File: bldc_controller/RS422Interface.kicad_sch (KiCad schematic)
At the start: 2 parts, among them U8 SN65HVD35DR

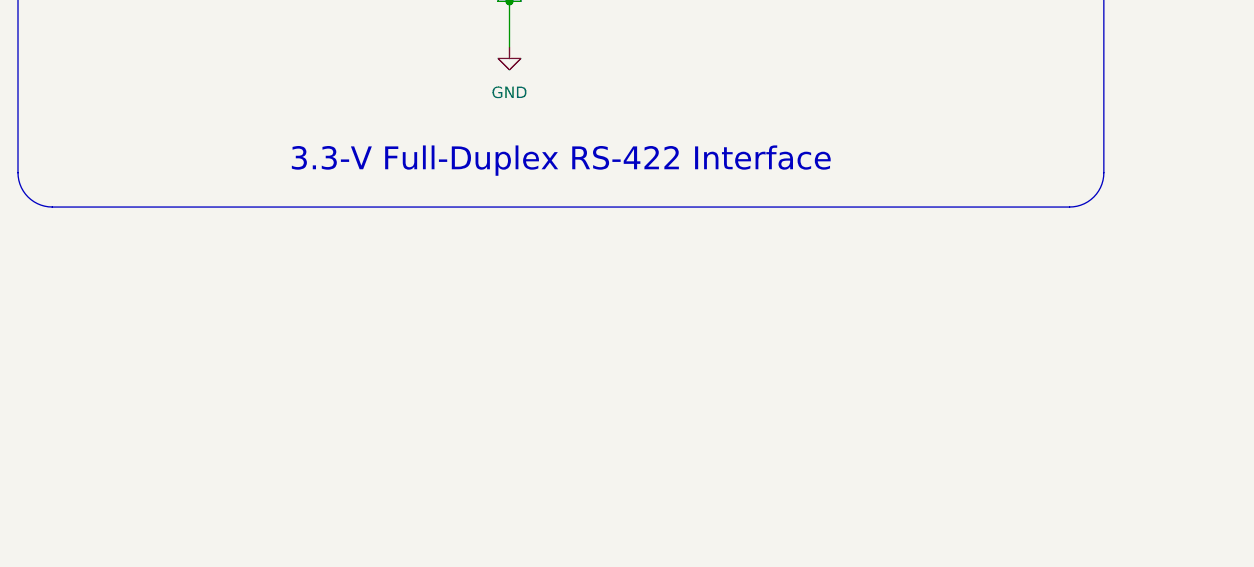
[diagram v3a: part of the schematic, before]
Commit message: Added TVS diodes to all interfaces
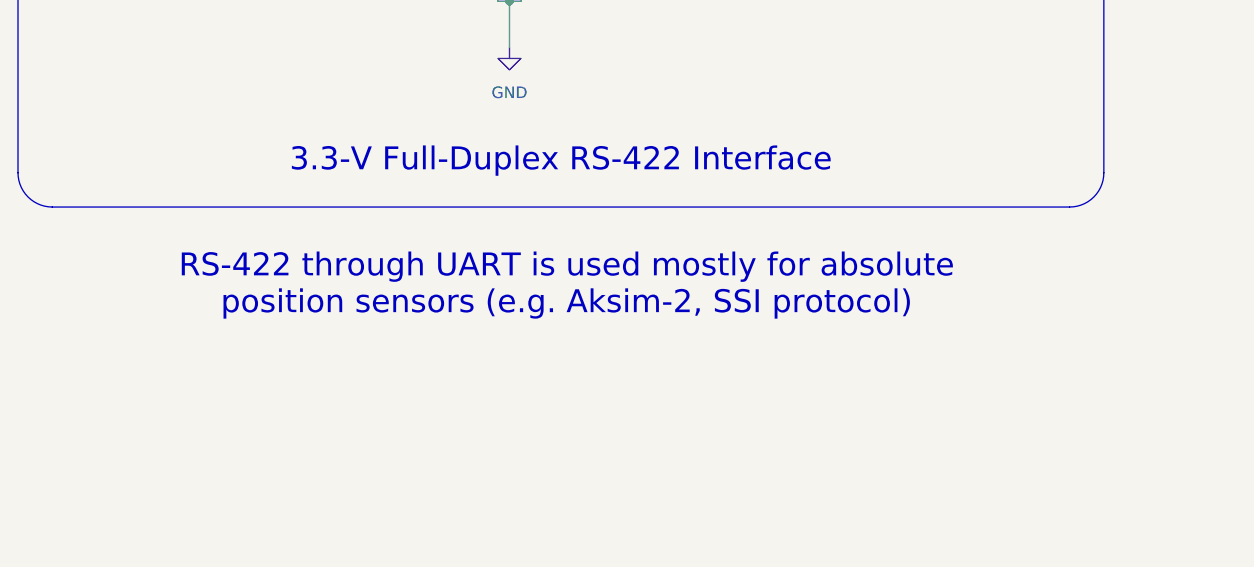
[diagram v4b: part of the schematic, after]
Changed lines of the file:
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@@
     (effects (font (size 1.27 1.27) (color 0 0 0 1)) (justify left))
+  )
+  (text_box "RS-422 through UART is used mostly for absolute position sensors (e.g. Aksim-2, SSI protocol)"
+    (at 92.71 133.35 0) (size 119.38 11.43)
+    (stroke (width -0.0001) (type default))
+    (fill (type none))
+    (effects (font (size 2.54 2.54) (color 0 0 0 1)) (justify bottom))
   )
   (text_box "3.3-V Full-Duplex RS-422 Interface"

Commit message: might have fixed net issue, added dxf and svgs
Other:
- moved on the sheet: C91, U8

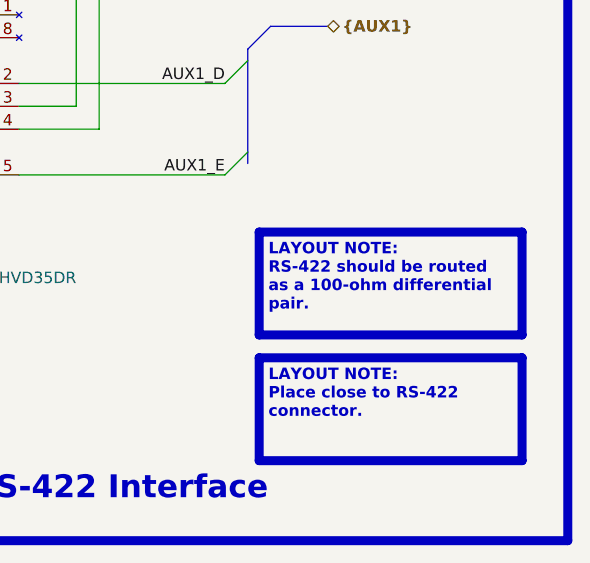
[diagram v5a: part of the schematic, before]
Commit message: added chassis connection to connector MP. Might need to change design rules to be compatible with low-cost PCBWay
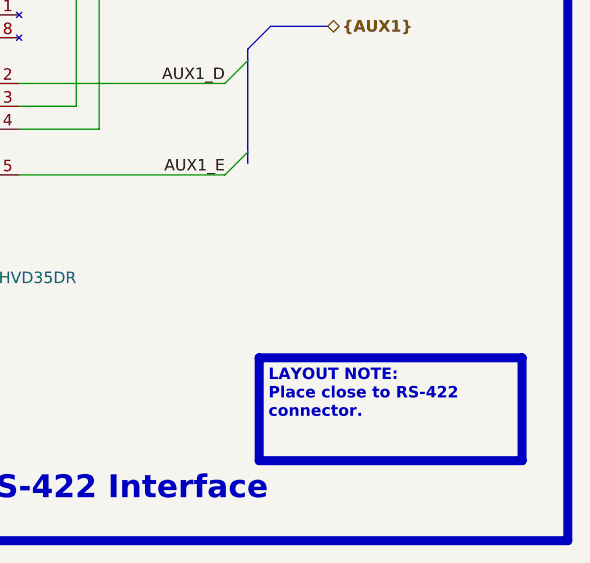
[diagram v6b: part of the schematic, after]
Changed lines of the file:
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@@
     (comment 3 "Author: Vincent Nguyen")
   )
-  (junction (at 146.05 104.14) (diameter 0) (color 0 0 0 0)
+  (junction (at 146.05 104.14) (diameter 0) (color 0 0 0 1)
   )
   (junction (at 147.32 54.61) (diameter 0) (color 0 0 0 0)
@@
   )
   (wire (pts (xy 146.05 104.14) (xy 147.32 104.14))
-    (stroke (width 0) (type default))
+    (stroke (width 0.381) (type default) (color 0 0 0 1))
   )
   (wire (pts (xy 147.32 54.61) (xy 147.32 62.23))
@@
   )
   (wire (pts (xy 144.78 104.14) (xy 144.78 102.87))
-    (stroke (width 0) (type default))
+    (stroke (width 0.381) (type default) (color 0 0 0 1))
   )
   (wire (pts (xy 144.78 62.23) (xy 144.78 64.77))
@@
   )
   (wire (pts (xy 128.27 64.77) (xy 128.27 62.23))
-    (stroke (width 0) (type default))
+    (stroke (width 0.381) (type default) (color 0 0 0 1))
   )
   (wire (pts (xy 128.27 54.61) (xy 147.32 54.61))
@@
   )
   (wire (pts (xy 147.32 102.87) (xy 147.32 104.14))
-    (stroke (width 0) (type default))
+    (stroke (width 0.381) (type default) (color 0 0 0 1))
   )
   (wire (pts (xy 162.56 62.23) (xy 179.07 62.23))
@@
   )
   (wire (pts (xy 146.05 104.14) (xy 144.78 104.14))
-    (stroke (width 0) (type default))
+    (stroke (width 0.381) (type default) (color 0 0 0 1))
   )
   (wire (pts (xy 146.05 109.22) (xy 146.05 104.14))
-    (stroke (width 0) (type default))
+    (stroke (width 0.381) (type default) (color 0 0 0 1))
   )
   (rectangle (start 82.55 41.91) (end 217.17 130.81)
@@
     (effects (font (face "Arial") (size 1.27 1.27) (color 0 0 0 1)) (justify left top))
   )
-  (text_box "LAYOUT NOTE:\nRS-422 should be routed as a 100-ohm differential pair."
-    (at 182.88 96.52 0) (size 29.21 11.43)
-    (stroke (width 1) (type solid) (color 0 0 255 1))
-    (fill (type none))
-    (effects (font (face "Arial") (size 1.27 1.27) (thickness 0.4) bold (color 0 0 255 1)) (justify left top))
-  )
   (text_box "DESIGN NOTE:\n100-ohm termination in Interconnects sheet."

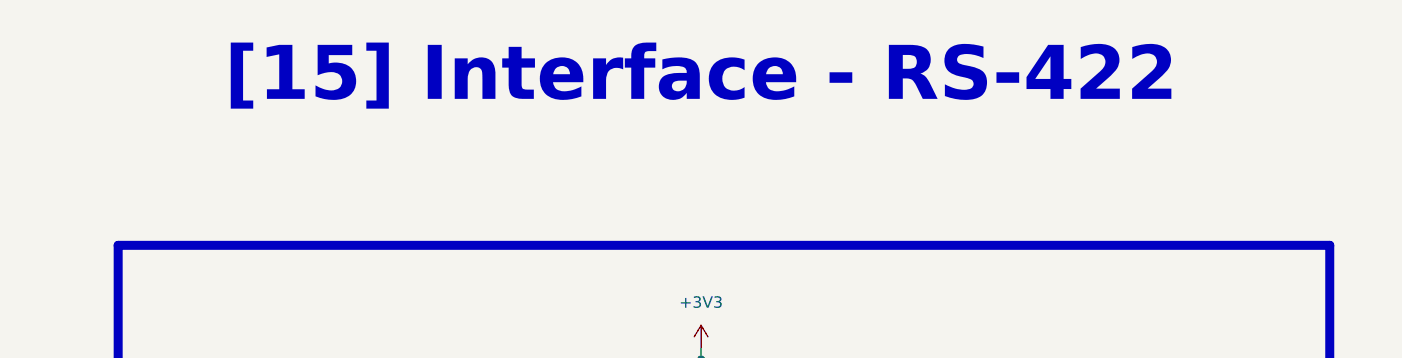
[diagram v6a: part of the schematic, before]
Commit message: Replaced 3v3 buck with WSON package alternative. Will back-annotate components
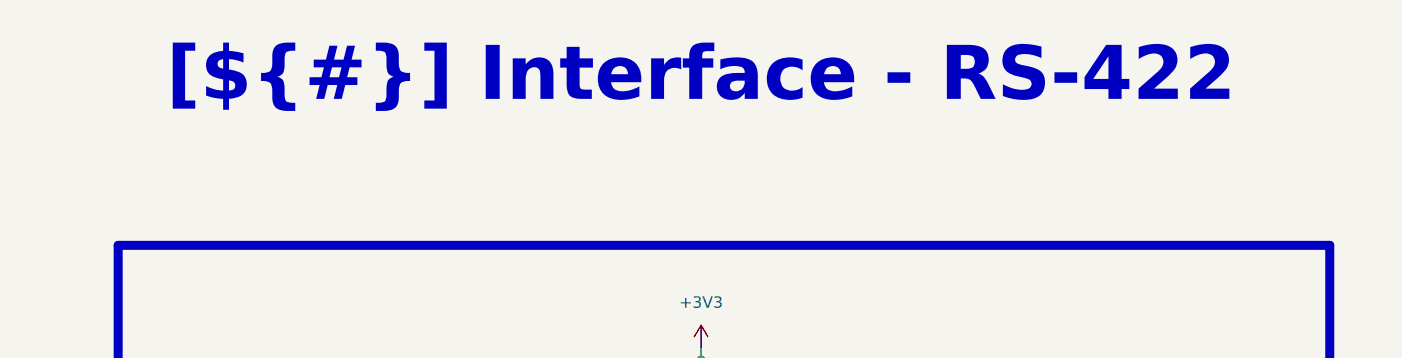
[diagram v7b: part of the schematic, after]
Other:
- company: EPFL Xplore -> ${COMPANY}
- title: RS-422 Interface -> Interface - RS-422
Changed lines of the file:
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@@
   (paper "A4")
   (title_block
-    (title "RS-422 Interface")
+    (title "Interface - RS-422")
     (date "2023-10-15")
-    (rev "1.0")
-    (company "EPFL Xplore")
-    (comment 3 "Author: Vincent Nguyen")
+    (rev "${REVISION}")
+    (company "${COMPANY}")
+    (comment 3 "Author: ${AUTHOR}")
   )
-  (junction (at 146.05 104.14) (diameter 0) (color 0 0 0 1)
+  (junction (at 146.05 104.14) (diameter 0) (color 0 0 0 0)
   )
   (junction (at 147.32 54.61) (diameter 0) (color 0 0 0 0)
@@
   )
   (wire (pts (xy 146.05 104.14) (xy 147.32 104.14))
-    (stroke (width 0.381) (type default) (color 0 0 0 1))
+    (stroke (width 0) (type default))
   )
   (wire (pts (xy 147.32 54.61) (xy 147.32 62.23))
@@
   )
   (wire (pts (xy 144.78 104.14) (xy 144.78 102.87))
-    (stroke (width 0.381) (type default) (color 0 0 0 1))
+    (stroke (width 0) (type default))
   )
   (wire (pts (xy 144.78 62.23) (xy 144.78 64.77))
@@
   )
   (wire (pts (xy 128.27 64.77) (xy 128.27 62.23))
-    (stroke (width 0.381) (type default) (color 0 0 0 1))
+    (stroke (width 0) (type default))
   )
   (wire (pts (xy 128.27 54.61) (xy 147.32 54.61))
@@
   )
   (wire (pts (xy 147.32 102.87) (xy 147.32 104.14))
-    (stroke (width 0.381) (type default) (color 0 0 0 1))
+    (stroke (width 0) (type default))
   )
   (wire (pts (xy 162.56 62.23) (xy 179.07 62.23))
@@
   )
   (wire (pts (xy 146.05 104.14) (xy 144.78 104.14))
-    (stroke (width 0.381) (type default) (color 0 0 0 1))
+    (stroke (width 0) (type default))
   )
   (wire (pts (xy 146.05 109.22) (xy 146.05 104.14))
-    (stroke (width 0.381) (type default) (color 0 0 0 1))
+    (stroke (width 0) (type default))
   )
   (rectangle (start 82.55 41.91) (end 217.17 130.81)
@@
     (effects (font (face "Times New Roman") (size 2.54 2.54) (thickness 0.508) bold (color 162 22 34 1)) (justify bottom))
   )
-  (text_box "[15] Interface - RS-422"
+  (text_box "[${#}] ${TITLE}"
     (at 78.74 16.51 0) (size 137.16 12.7)
     (stroke (width -0.0001) (type default))

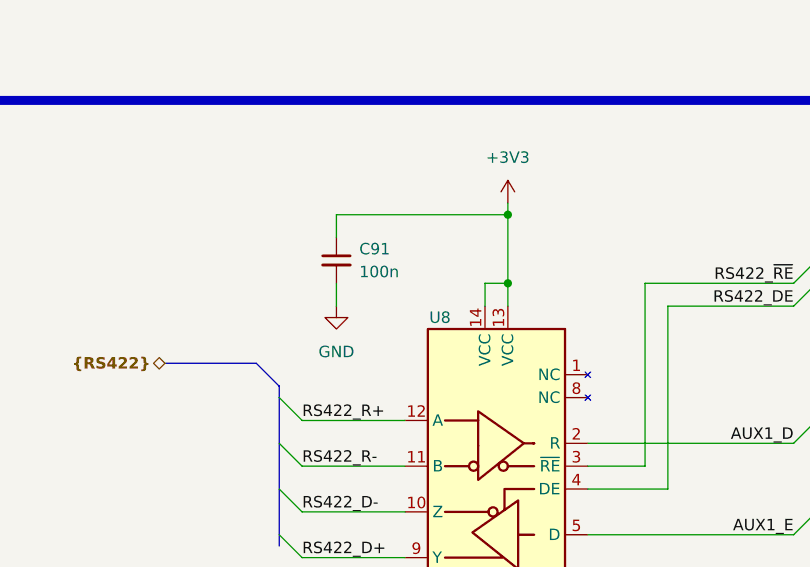
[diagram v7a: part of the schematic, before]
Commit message: routed all signals. TODO: redo all power polygons and ensure good return paths/reference. Added 3d models
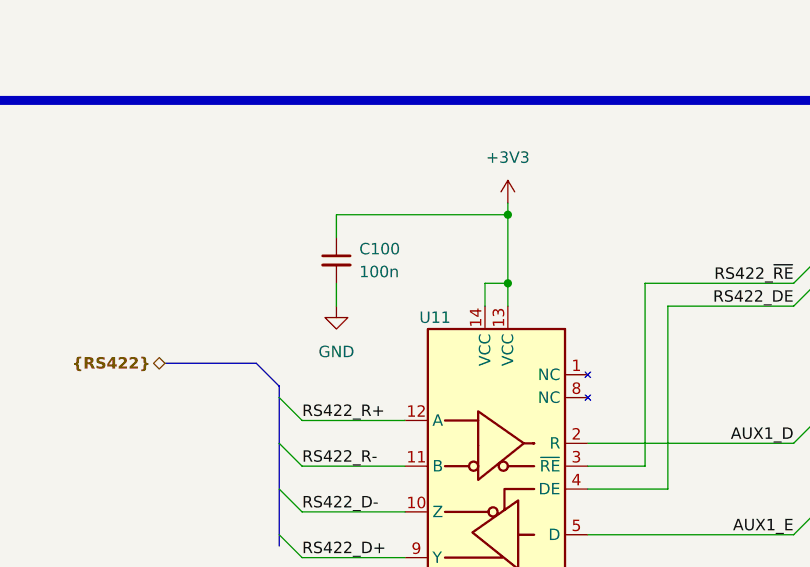
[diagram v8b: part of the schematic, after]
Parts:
- renumbered C91 to C100, U8 to U11
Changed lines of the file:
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@@
   (symbol (lib_id "power:+3V3") (at 147.32 53.34 0) (unit 1)
     (in_bom yes) (on_board yes) (dnp no) (fields_autoplaced)
-    (property "Reference" "#PWR068" (at 147.32 57.15 0)
+    (property "Reference" "#PWR052" (at 147.32 57.15 0)
       (effects (font (size 1.27 1.27)) hide)
     )
@@
       (project "bldc_controller"
         (path "/0650c7a8-acba-429c-9f8e-eec0baf0bc1c/fede4c36-00cc-4d3d-b71c-5243ba232202/a62105fd-dfaf-4ee0-a401-8aa0e7120758"
-          (reference "#PWR068") (unit 1)
+          (reference "#PWR052") (unit 1)
         )
       )
@@
   (symbol (lib_id "Device:C_Small") (at 128.27 59.69 0) (unit 1)
     (in_bom yes) (on_board yes) (dnp no) (fields_autoplaced)
-    (property "Reference" "C91" (at 130.81 58.4263 0)
+    (property "Reference" "C100" (at 130.81 58.4263 0)
       (effects (font (size 1.27 1.27)) (justify left))
     )
@@
       (project "bldc_controller"
         (path "/0650c7a8-acba-429c-9f8e-eec0baf0bc1c/fede4c36-00cc-4d3d-b71c-5243ba232202/a62105fd-dfaf-4ee0-a401-8aa0e7120758"
-          (reference "C91") (unit 1)
+          (reference "C100") (unit 1)
         )
       )
@@
   (symbol (lib_id "power:GND") (at 128.27 64.77 0) (unit 1)
     (in_bom yes) (on_board yes) (dnp no) (fields_autoplaced)
-    (property "Reference" "#PWR066" (at 128.27 71.12 0)
+    (property "Reference" "#PWR050" (at 128.27 71.12 0)
       (effects (font (size 1.27 1.27)) hide)
     )
@@
       (project "bldc_controller"
         (path "/0650c7a8-acba-429c-9f8e-eec0baf0bc1c/fede4c36-00cc-4d3d-b71c-5243ba232202/a62105fd-dfaf-4ee0-a401-8aa0e7120758"
-          (reference "#PWR066") (unit 1)
+          (reference "#PWR050") (unit 1)
         )
       )
@@
   (symbol (lib_id "power:GND") (at 146.05 109.22 0) (unit 1)
     (in_bom yes) (on_board yes) (dnp no) (fields_autoplaced)
-    (property "Reference" "#PWR067" (at 146.05 115.57 0)
+    (property "Reference" "#PWR051" (at 146.05 115.57 0)
       (effects (font (size 1.27 1.27)) hide)
     )
@@
       (project "bldc_controller"
         (path "/0650c7a8-acba-429c-9f8e-eec0baf0bc1c/fede4c36-00cc-4d3d-b71c-5243ba232202/a62105fd-dfaf-4ee0-a401-8aa0e7120758"
-          (reference "#PWR067") (unit 1)
+          (reference "#PWR051") (unit 1)
         )
       )
@@
   (symbol (lib_id "0_interface_uart:SN65HVD35DR") (at 146.05 85.09 0) (mirror y) (unit 1)
     (in_bom yes) (on_board yes) (dnp no)
-    (property "Reference" "U8" (at 140.97 66.04 0)
+    (property "Reference" "U11" (at 140.97 66.04 0)
       (effects (font (size 1.27 1.27)) (justify left))
     )
@@
       (project "bldc_controller"
         (path "/0650c7a8-acba-429c-9f8e-eec0baf0bc1c/fede4c36-00cc-4d3d-b71c-5243ba232202/a62105fd-dfaf-4ee0-a401-8aa0e7120758"
-          (reference "U8") (unit 1)
+          (reference "U11") (unit 1)
         )
       )
